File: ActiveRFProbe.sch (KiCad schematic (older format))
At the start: 40 parts, among them J1 Conn_01x01, J16 Conn_01x01, J17 Conn_01x01, J18 Conn_01x01, J19 Conn_01x01, J2 Conn_01x01, J20 Conn_01x01, J21 Conn_01x01, J22 Conn_01x01, J23 Conn_01x01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

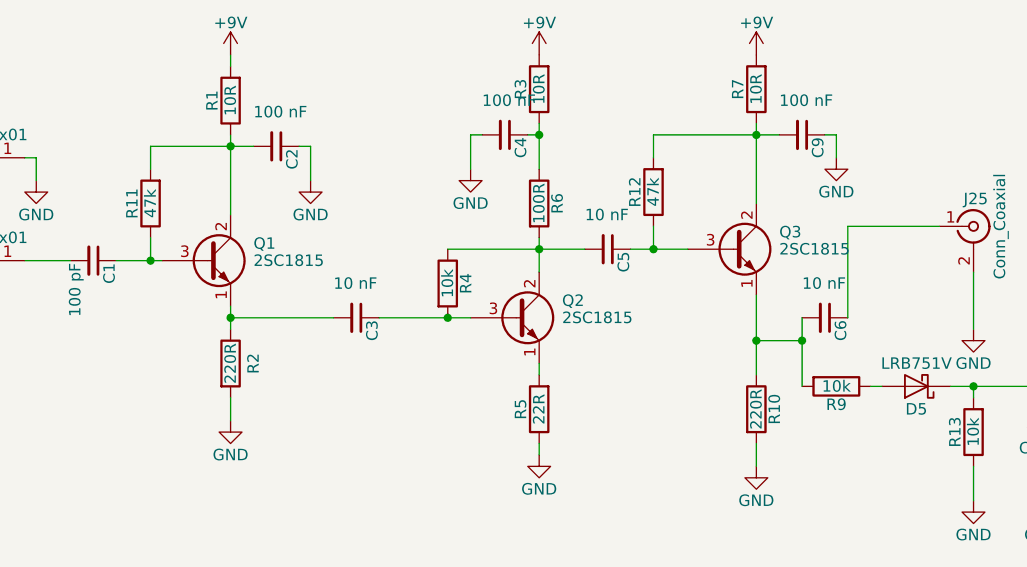
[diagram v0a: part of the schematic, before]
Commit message: Changed to 2SC3356
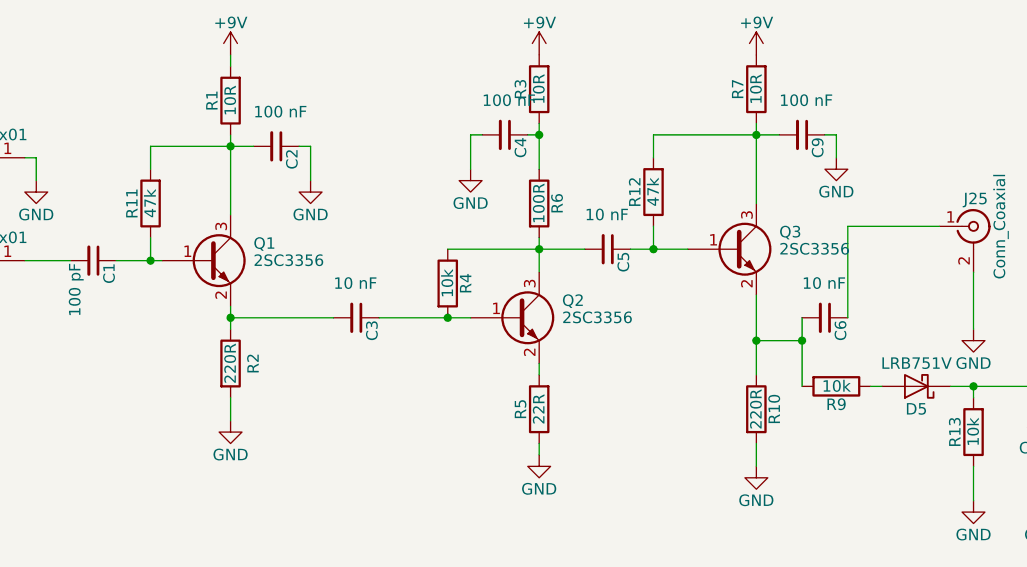
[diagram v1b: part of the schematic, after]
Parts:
- removed Q1, Q2, Q3: 2SC1815, TO_SOT_Packages_SMD:SOT-89-3_Handsoldering, symbol 2SC1815
- added Q1, Q2, Q3: 2SC3356, TO_SOT_Packages_SMD:SOT-23, symbol MMBT3904
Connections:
- net at C1.1, R11.1: now also Q1.1 (B)
- net at C3.2, R2.1: now also Q1.2 (E)
- net at C3.1, R4.2: now also Q2.1 (B)
- net at C5.2, R4.1, R6.2: now also Q2.3 (C)
- net at R5.2: now also Q2.2 (E)
- net at C5.1, R12.1: now also Q3.1 (B)
- net at C6.2, R10.1, R9.2: now also Q3.2 (E)
- net at C2.2, R1.1, R11.2: now also Q1.3 (C)
- net at C9.2, R12.2, R7.1: now also Q3.3 (C)
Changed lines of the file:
@@
 	5050 3350 5600 3350
-$Comp
-L 2SC1815 Q3
-U 1 1 5EA03BFC
-P 5400 3850
-F 0 "Q3" H 5600 3925 50  0000 L CNN
-F 1 "2SC1815" H 5600 3850 50  0000 L CNN
-F 2 "TO_SOT_Packages_SMD:SOT-89-3_Handsoldering" H 5600 3775 50  0001 L CIN
-F 3 "" H 5400 3850 50  0001 L CNN
-F 4 "C193446" H 5400 3850 60  0001 C CNN "LCSC"
-	1    5400 3850
-	1    0    0    -1
-$EndComp
-$Comp
-L 2SC1815 Q1
-U 1 1 5EA03D75
-P 3100 3900
-F 0 "Q1" H 3300 3975 50  0000 L CNN
-F 1 "2SC1815" H 3300 3900 50  0000 L CNN
-F 2 "TO_SOT_Packages_SMD:SOT-89-3_Handsoldering" H 3300 3825 50  0001 L CIN
-F 3 "" H 3100 3900 50  0001 L CNN
-F 4 "C193446" H 3100 3900 60  0001 C CNN "LCSC"
-	1    3100 3900
-	1    0    0    -1
-$EndComp
-$Comp
-L 2SC1815 Q2
-U 1 1 5EA03E80
-P 4450 4150
-F 0 "Q2" H 4650 4225 50  0000 L CNN
-F 1 "2SC1815" H 4650 4150 50  0000 L CNN
-F 2 "TO_SOT_Packages_SMD:SOT-89-3_Handsoldering" H 4650 4075 50  0001 L CIN
-F 3 "" H 4450 4150 50  0001 L CNN
-F 4 "C193446" H 4450 4150 60  0001 C CNN "LCSC"
-	1    4450 4150
-	1    0    0    -1
-$EndComp
 $Comp
 L R R1
@@
 	-1   0    0    1
 $EndComp
+$Comp
+L MMBT3904 Q1
+U 1 1 5EA1B541
+P 3100 3900
+F 0 "Q1" H 3300 3975 50  0000 L CNN
+F 1 "2SC3356" H 3300 3900 50  0000 L CNN
+F 2 "TO_SOT_Packages_SMD:SOT-23" H 3300 3825 50  0001 L CIN
+F 3 "" H 3100 3900 50  0001 L CNN
+F 4 "C9659" H 3100 3900 60  0001 C CNN "LCSC"
+	1    3100 3900
+	1    0    0    -1
+$EndComp
+$Comp
+L MMBT3904 Q2
+U 1 1 5EA1B664
+P 4450 4150
+F 0 "Q2" H 4650 4225 50  0000 L CNN
+F 1 "2SC3356" H 4650 4150 50  0000 L CNN
+F 2 "TO_SOT_Packages_SMD:SOT-23" H 4650 4075 50  0001 L CIN
+F 3 "" H 4450 4150 50  0001 L CNN
+F 4 "C9659" H 4450 4150 60  0001 C CNN "LCSC"
+	1    4450 4150
+	1    0    0    -1
+$EndComp
+$Comp
+L MMBT3904 Q3
+U 1 1 5EA1B78D
+P 5400 3850
+F 0 "Q3" H 5600 3925 50  0000 L CNN
+F 1 "2SC3356" H 5600 3850 50  0000 L CNN
+F 2 "TO_SOT_Packages_SMD:SOT-23" H 5600 3775 50  0001 L CIN
+F 3 "" H 5400 3850 50  0001 L CNN
+F 4 "C9659" H 5400 3850 60  0001 C CNN "LCSC"
+	1    5400 3850
+	1    0    0    -1
+$EndComp
 $EndSCHEMATC

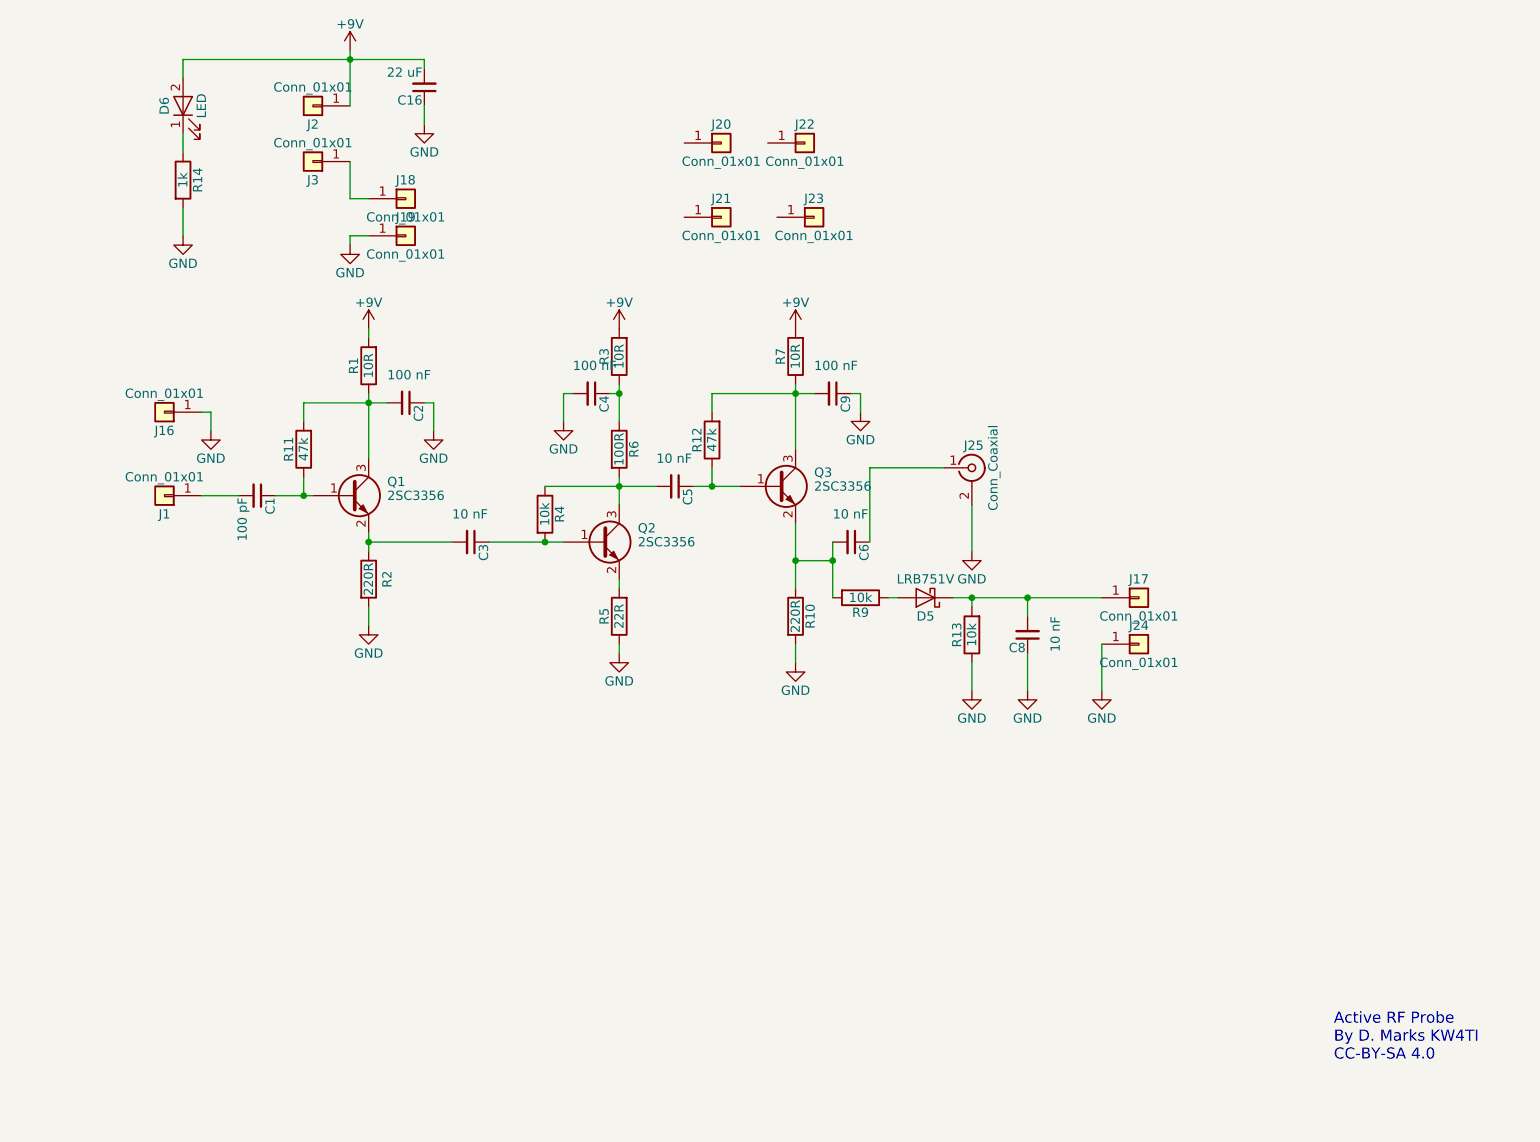
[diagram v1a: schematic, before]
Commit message: Added LCSC part numbers, added cutout notched, added series base resistors to emitter followers
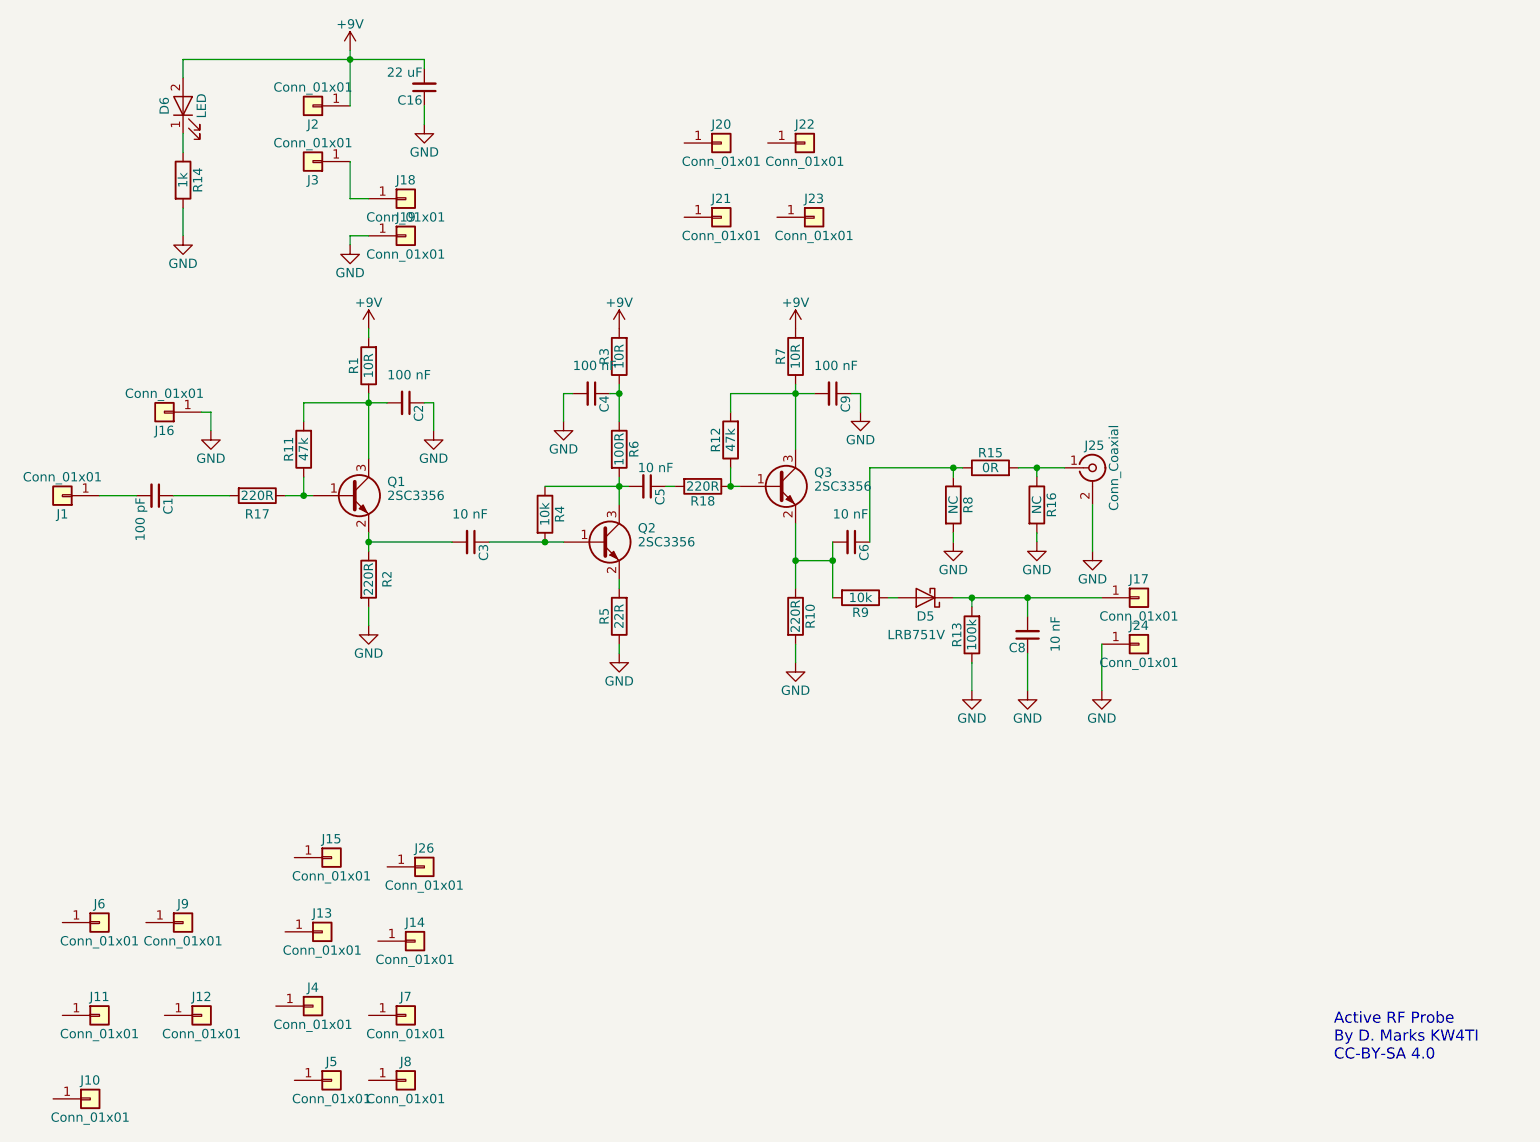
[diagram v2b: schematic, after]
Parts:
- added J10, J11, J12, J13, J14, J15, J26, J4, J5, J6, J7, J8, J9: Conn_01x01, ActiveRFProbe:BigSlot, symbol Conn_01x01
- added R15: 0R, Resistors_SMD:R_0805_HandSoldering, symbol R
- added R16, R8: NC, Resistors_SMD:R_0805_HandSoldering, symbol R
- added R17, R18: 220R, Resistors_SMD:R_0805_HandSoldering, symbol R
- R13: value 10k -> 100k; LCSC C17414 -> C17407
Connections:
- net GND: now also R16.2, R8.2
- net at Q1.1 (B), R11.1: now also R17.1; no longer C1.1
- net at Q3.1 (B), R12.1: now also R18.1; no longer C5.1
- net at C6.1: now also R15.1, R8.1; no longer J25.1 (In)
- new net: C1.1, R17.2
- new net: C5.1, R18.2
- new net: J25.1 (In), R15.2, R16.1
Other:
- moved on the sheet: C1, C5, J1, J25, R12

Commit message: Modified base resistors
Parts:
- R17, R18: value 220R -> 22R; LCSC C17557 -> C17561
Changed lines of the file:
@@
 P 2600 3900
 F 0 "R17" V 2700 3900 50  0000 C CNN
-F 1 "220R" V 2600 3900 50  0000 C CNN
+F 1 "22R" V 2600 3900 50  0000 C CNN
 F 2 "Resistors_SMD:R_0805_HandSoldering" V 2530 3900 50  0001 C CNN
 F 3 "" H 2600 3900 50  0001 C CNN
-F 4 "C17557" V 2600 3900 60  0001 C CNN "LCSC"
+F 4 "C17561" V 2600 3900 60  0001 C CNN "LCSC"
 	1    2600 3900
 	0    1    1    0
@@
 P 5000 3850
 F 0 "R18" V 5080 3850 50  0000 C CNN
-F 1 "220R" V 5000 3850 50  0000 C CNN
+F 1 "22R" V 5000 3850 50  0000 C CNN
 F 2 "Resistors_SMD:R_0805_HandSoldering" V 4930 3850 50  0001 C CNN
 F 3 "" H 5000 3850 50  0001 C CNN
-F 4 "C17557" V 5000 3850 60  0001 C CNN "LCSC"
+F 4 "C17561" V 5000 3850 60  0001 C CNN "LCSC"
 	1    5000 3850
 	0    1    1    0
